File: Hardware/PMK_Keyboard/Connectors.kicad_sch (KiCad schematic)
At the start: 22 parts, among them J101 USB4510-03-1-A, Q111 ZXMN3B01F, Q112 ZXMN3B01F, Q113 PMOS, Q114 PMOS

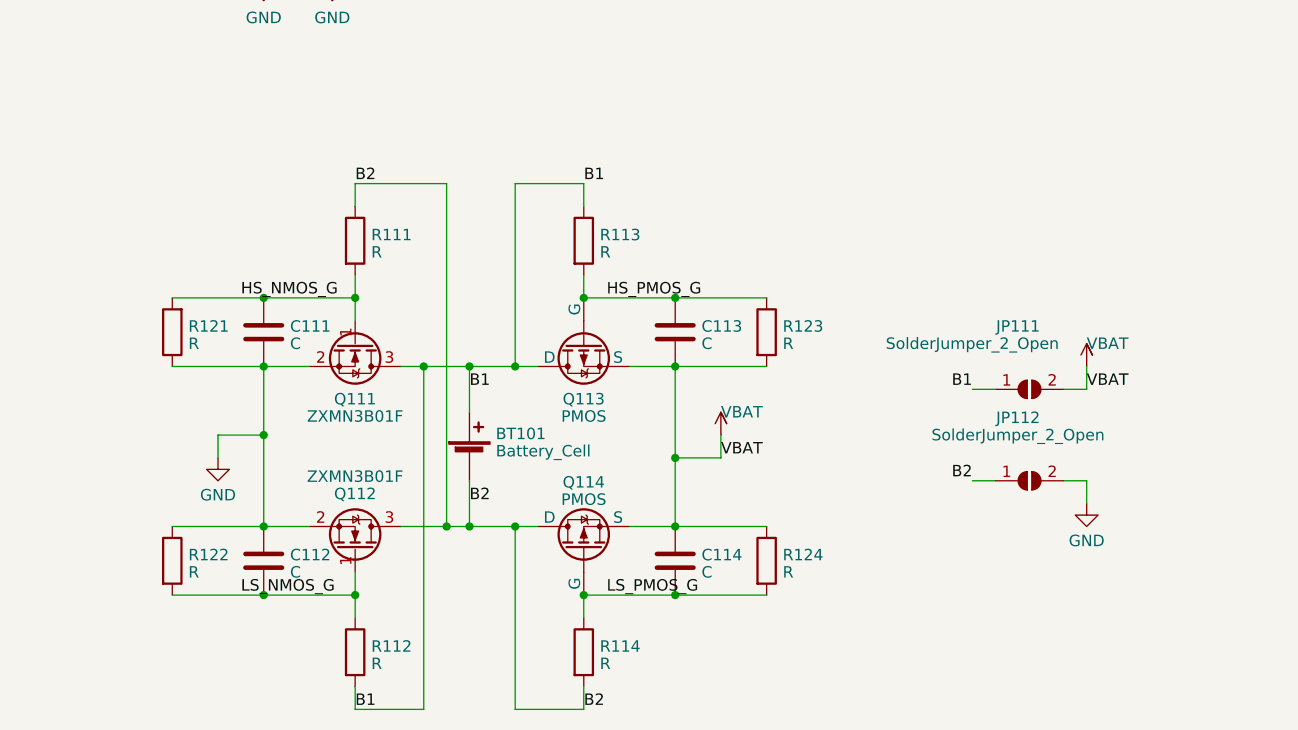
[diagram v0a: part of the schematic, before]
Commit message: removed anti reverse polarity system
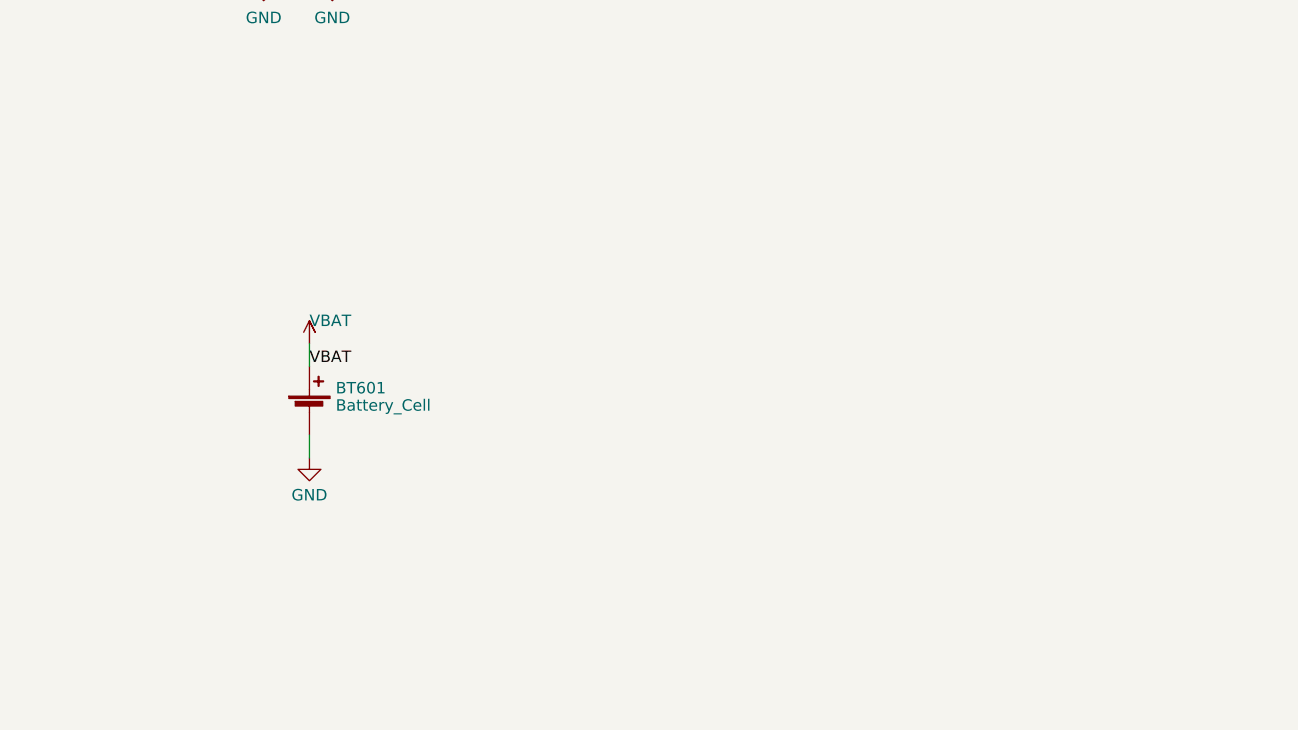
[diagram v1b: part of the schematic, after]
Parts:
- removed BT101: Battery_Cell, symbol Device:Battery_Cell
- removed C111, C112, C113, C114: C, symbol Component_lib:C
- removed JP111, JP112: SolderJumper_2_Open, symbol Jumper:SolderJumper_2_Open
- removed Q111, Q112: ZXMN3B01F, Package_TO_SOT_SMD:SOT-23, symbol Component_lib:ZXMN3B01F
- removed Q113, Q114: PMOS, symbol Simulation_SPICE:PMOS
- removed R111, R112, R113, R114, R121, R122, R123, R124: R, symbol Component_lib:R
- added BT601: Battery_Cell, Component_lib:BatteryHolder_Keystone_1042_1x18650_DUALSIDE, symbol Device:Battery_Cell
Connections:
- net GND: now also BT601.2 (-)
- net VBAT: now also BT601.1 (+)

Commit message: quick update
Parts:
- renumbered BT601 to BT101
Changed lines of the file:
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@@
   (symbol (lib_id "Device:Battery_Cell") (at 48.26 137.16 0) (unit 1)
     (in_bom yes) (on_board yes) (dnp no) (fields_autoplaced)
-    (property "Reference" "BT601" (at 51.181 134.4843 0)
+    (property "Reference" "BT101" (at 51.181 134.4843 0)
       (effects (font (size 1.27 1.27)) (justify left))
     )
@@
       (project "PMK_Keyboard"
         (path "/c3b08055-08a5-4979-9bf8-f36ab0917722/cf9fd53d-a626-44ae-9c40-26b02d8cda14"
-          (reference "BT601") (unit 1)
+          (reference "BT101") (unit 1)
         )
       )
